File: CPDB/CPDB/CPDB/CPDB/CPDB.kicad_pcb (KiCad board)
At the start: 2 copper layers, 38 x 38 mm, 26 parts, among them J1 Conn_01x02_Pin, J2 Conn_01x04_Pin, U1 INA219BxDCN, U2 TPS54302DDCR, U3 TPS563240DDCR

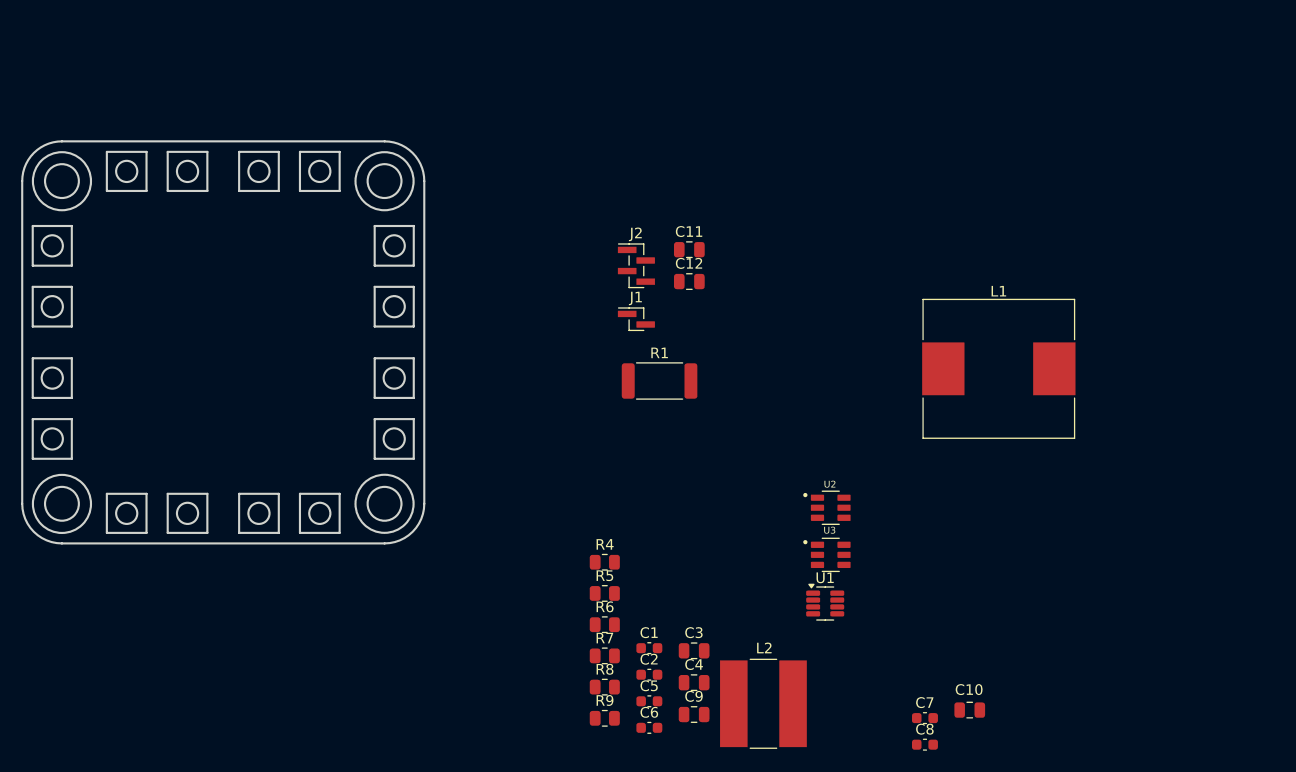
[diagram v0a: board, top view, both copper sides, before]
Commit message: gruplama yapıldı, indüktörler değişti
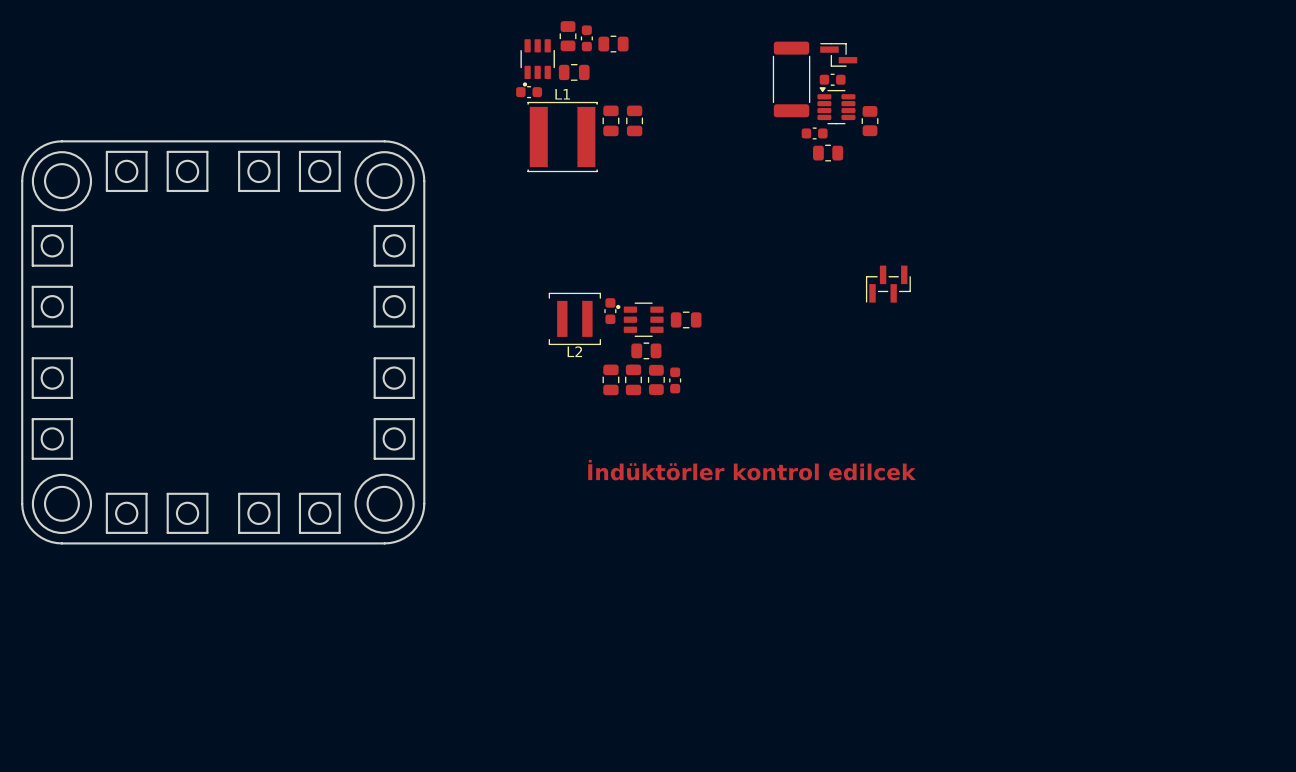
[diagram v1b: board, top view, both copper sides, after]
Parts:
- L1: footprint Inductor_SMD:L_Chilisin_BMRF00131350 -> Inductor_SMD:L_Sunlord_SWPA6045S
- L2: footprint Inductor_SMD:L_Bourns-SRN8040_8x8.15mm -> Inductor_SMD:L_Coilcraft_XAL4020-XXX
- moved C8 74.0 mm to (182.9, 77.0), turned to 90 degrees
- moved R9 64.6 mm to (181.1, 76.8), turned to 90 degrees
- moved C10 64.1 mm to (187.4, 84.8), turned to 90 degrees
- moved C6 61.1 mm to (177.4, 82.1)
- moved R8 60.8 mm to (185.4, 77.6), turned to 180 degrees
- moved C4 58.8 mm to (181.7, 80.2)
- moved C1 56.5 mm to (206.1, 80.9)
- moved C2 53.5 mm to (204.4, 86.0)
- moved U2 50.6 mm to (178.2, 79.0), turned to 90 degrees
- moved R4 48.6 mm to (209.6, 84.8), turned to 90 degrees
- moved C7 48.6 mm to (185.1, 102.8), turned to -90 degrees
- moved U1 46.9 mm to (206.5, 83.5)
- moved L1 46.7 mm to (180.6, 86.3)
- moved R5 46.7 mm to (205.7, 87.9)
- moved L2 40.5 mm to (181.7, 103.5), turned to 180 degrees
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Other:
- board text added: "İndüktörler kontrol edilcek"

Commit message: ESC pin placement.
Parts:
- added J10: Conn_01x01_Pin, Connector_Samtec_HPM_THT:Samtec_HPM-01-05-x-S_Straight_1x01_Pitch5.08mm, F.Cu at (236.1, 106.4)
- added J3: Conn_01x01_Pin, Connector_Samtec_HPM_THT:Samtec_HPM-01-05-x-S_Straight_1x01_Pitch5.08mm, F.Cu at (244.5, 98.3)
- added J4: Conn_01x01_Pin, Connector_Samtec_HPM_THT:Samtec_HPM-01-05-x-S_Straight_1x01_Pitch5.08mm, F.Cu at (244.5, 92.7)
- added J5: Conn_01x01_Pin, Connector_Samtec_HPM_THT:Samtec_HPM-01-05-x-S_Straight_1x01_Pitch5.08mm, F.Cu at (226.3, 122.2)
- added J6: Conn_01x01_Pin, Connector_Samtec_HPM_THT:Samtec_HPM-01-05-x-S_Straight_1x01_Pitch5.08mm, F.Cu at (230.9, 122.2)
- added J7: Conn_01x01_Pin, Connector_Samtec_HPM_THT:Samtec_HPM-01-05-x-S_Straight_1x01_Pitch5.08mm, F.Cu at (236.1, 92.6)
- added J8: Conn_01x01_Pin, Connector_Samtec_HPM_THT:Samtec_HPM-01-05-x-S_Straight_1x01_Pitch5.08mm, F.Cu at (236.1, 97.2)
- added J9: Conn_01x01_Pin, Connector_Samtec_HPM_THT:Samtec_HPM-01-05-x-S_Straight_1x01_Pitch5.08mm, F.Cu at (236.1, 101.8)
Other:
- outline, holes or cut-outs redrawn
